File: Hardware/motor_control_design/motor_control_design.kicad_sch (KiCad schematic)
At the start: 40 parts, among them J1 TYPE-C-31-M-12, J2 SWD, J3 VBAT, J4 GND, J5 FC_M/P, U1 STM32F401CCU6, U2 AMS1117-3.3, U3 LM2576S-3.3, Y1 16MHz

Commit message: Added Vbat Sensing schema to motor board
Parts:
- added R11: 29.4k, Resistor_SMD:R_0402_1005Metric, symbol Device:R
- added R12: 10k, Resistor_SMD:R_0402_1005Metric, symbol Device:R
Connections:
- net +3.3V: now also U1.12 (PA2)
- net +BATT: now also R11.1
- net GND: now also R12.2
- net VBatt_sense: now reaches U1.11 (PA1)
- net VBatt_sense: now also R11.2, R12.1
- no-connect marks 35 -> 33
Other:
- note added: "*Calculated based off of 3S 18650 pack 18650: 2.5V -> 4.2V | 12.6v -> 3.198v pack : 7.5V -> 12.6v | 7.5v -> 1.904v ADC range is 0v -> 3.3v"
- note added: "*Need to test LM2576 voltage stability under ext. motor load, and heavy downstream load If needed, we may need to create a seperate power source for VREF+. Not sure how, but we could use a LM2576-5V then use a cheap 3.3V LDO and a high precsision one"
- note added: "Battery Voltage Measure"

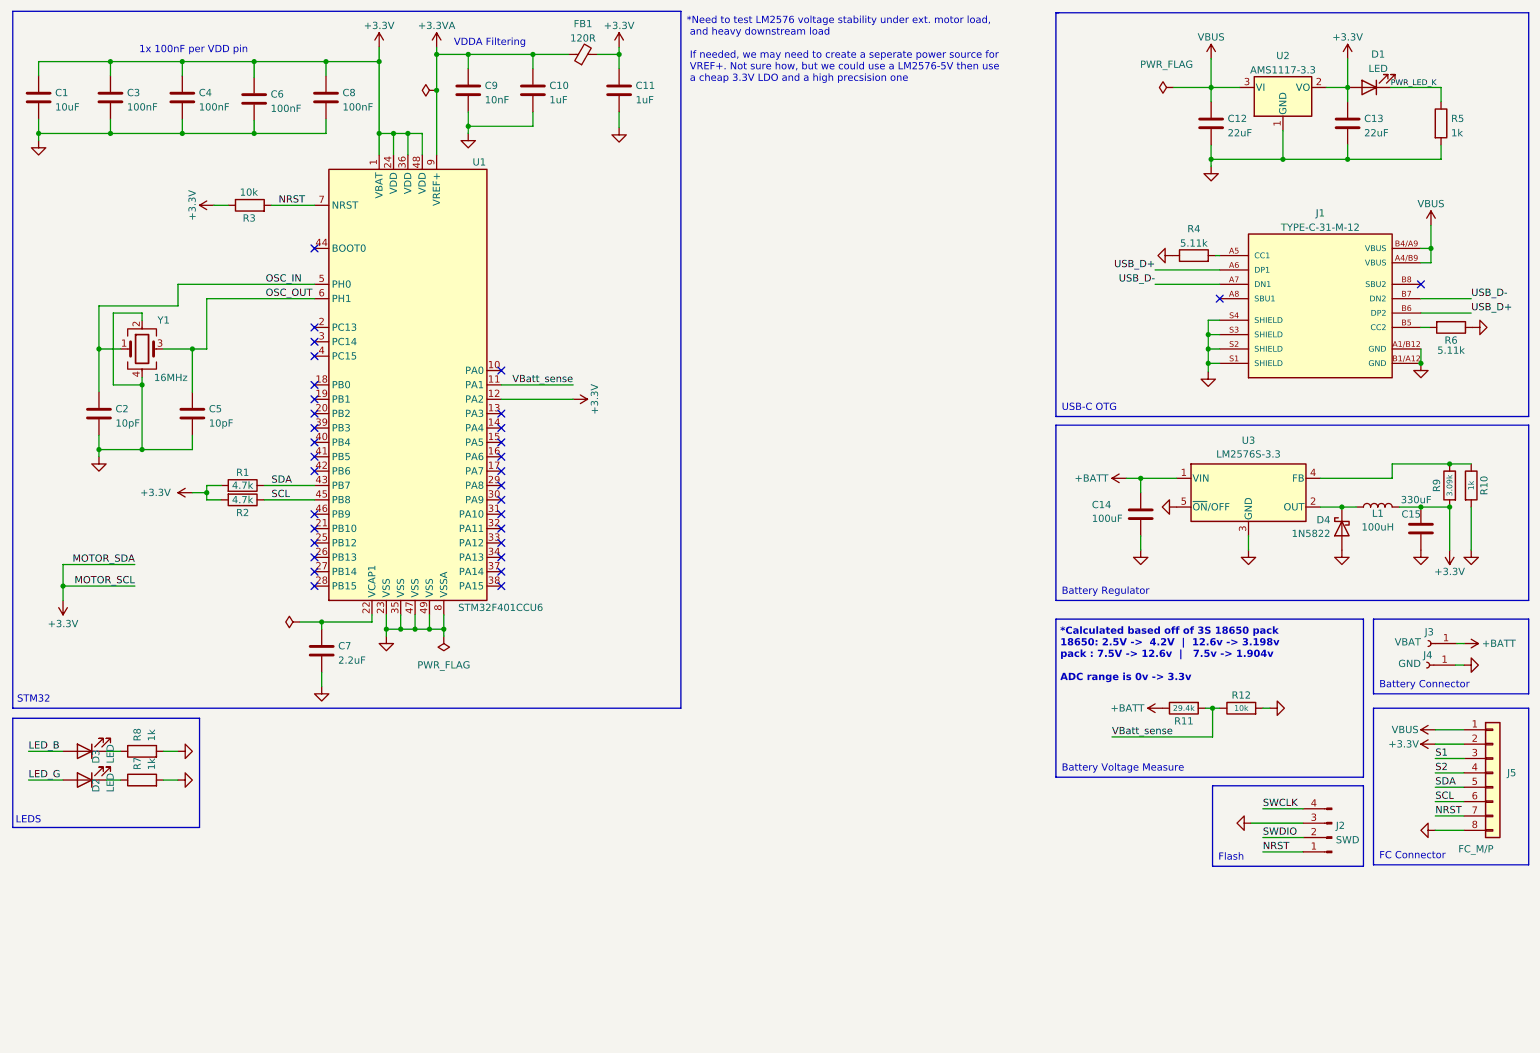
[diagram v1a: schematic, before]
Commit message: Added both H-Bridge schemas (pending testing)
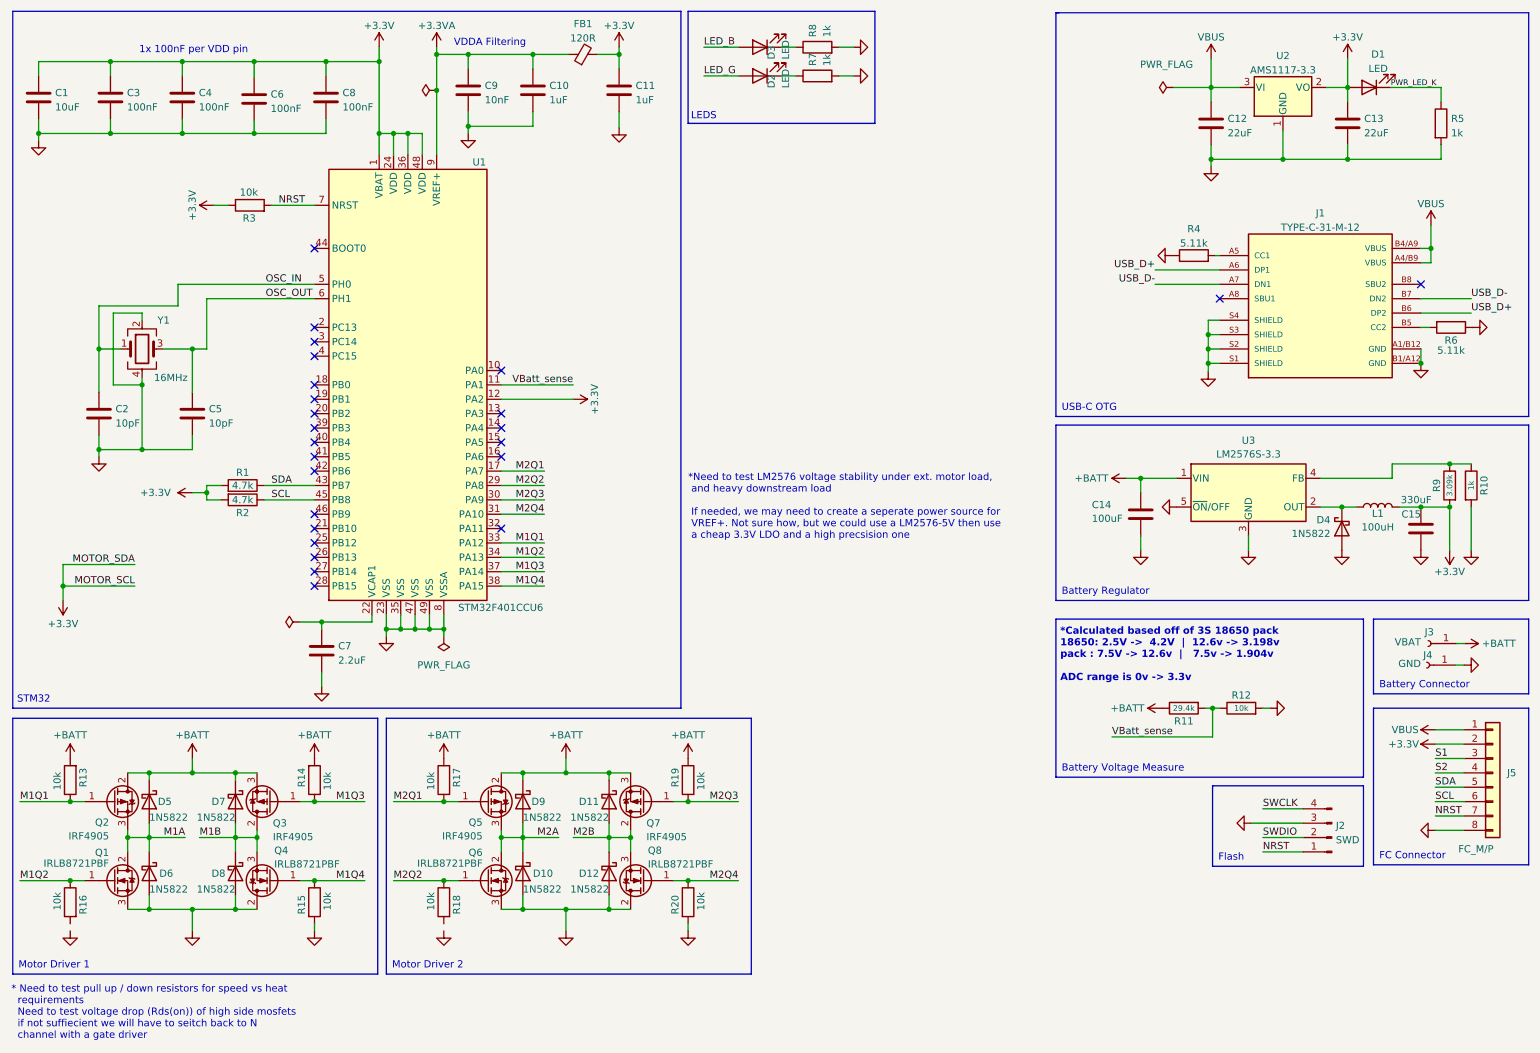
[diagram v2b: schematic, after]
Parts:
- added D10, D11, D12, D5, D6, D7, D8, D9: 1N5822, Diode_THT:D_DO-201AD_P15.24mm_Horizontal, symbol Diode:1N5822
- added Q1, Q4, Q6, Q8: IRLB8721PBF, Package_TO_SOT_THT:TO-220-3_Vertical, symbol Transistor_FET:IRLB8721PBF
- added Q2, Q3, Q5, Q7: IRF4905, Package_TO_SOT_THT:TO-220-3_Vertical, symbol Transistor_FET:IRF4905
- added R13, R14, R15, R16, R17, R18, R19, R20: 10k, Resistor_SMD:R_0402_1005Metric, symbol Device:R
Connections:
- net +BATT: now also D11.1 (K), D5.1 (K), D7.1 (K), D9.1 (K), Q2.2 (D), Q3.3 (S), Q5.2 (D), Q7.3 (S), R13.2, R14.2, R17.2, R19.2
- net GND: now also D10.2 (A), D12.2 (A), D6.2 (A), D8.2 (A), Q1.3 (S), Q4.2 (D), Q6.3 (S), Q8.2 (D), R15.2, R20.2
- net M2Q1: now reaches U1.17 (PA7)
- net M2Q1: now also Q5.1 (G), R17.1
- net M2Q2: now reaches U1.29 (PA8)
- net M2Q2: now also Q6.1 (G), R18.1
- net M2Q3: now reaches U1.30 (PA9)
- net M2Q3: now also Q7.1 (G), R19.1
- net M2Q4: now reaches U1.31 (PA10)
- net M2Q4: now also Q8.1 (G), R20.1
- net M1Q1: now reaches U1.33 (PA12)
- net M1Q1: now also Q2.1 (G), R13.1
- net M1Q2: now reaches U1.34 (PA13)
- net M1Q2: now also Q1.1 (G), R16.1
- net M1Q3: now reaches U1.37 (PA14)
- net M1Q3: now also Q3.1 (G), R14.1
- net M1Q4: now reaches U1.38 (PA15)
- net M1Q4: now also Q4.1 (G), R15.1
- new net M1A: D5.2 (A), D6.1 (K), Q1.2 (D), Q2.3 (S)
- new net M1B: D7.2 (A), D8.1 (K), Q3.2 (D), Q4.3 (S)
- new net M2A: D10.1 (K), D9.2 (A), Q5.3 (S), Q6.2 (D)
- new net M2B: D11.2 (A), D12.1 (K), Q7.2 (D), Q8.3 (S)
- no-connect marks 33 -> 25
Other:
- note added: "* Need to test pull up / down resistors for speed vs heat requirements Need to test voltage drop (Rds(on)) of high side mosfets if not suffiecient we will have to seitch back to N channel with a gate driver"
- note added: "Motor Driver 1"
- note added: "Motor Driver 2"
- moved on the sheet: D2, D3, R7, R8

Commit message: Finished motor controller schematic and routing
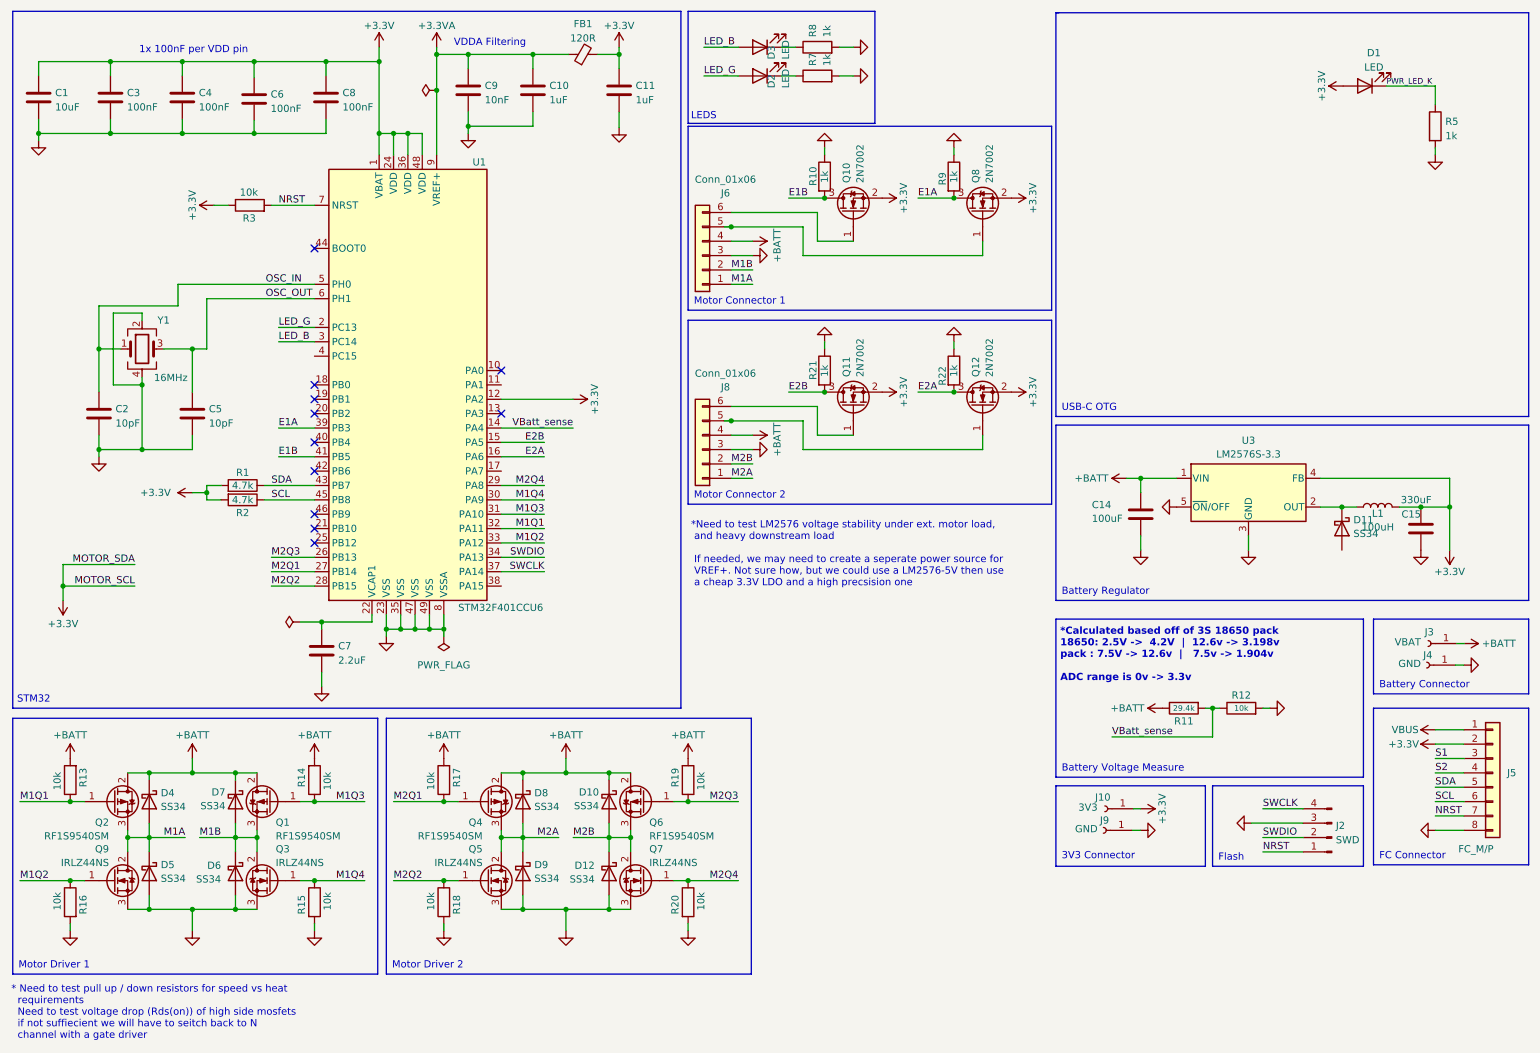
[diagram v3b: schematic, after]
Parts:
- removed C12, C13: 22uF, Capacitor_SMD:C_0805_2012Metric, symbol Device:C
- removed D10, D11, D12, D4, D5, D6, D7, D8, D9: 1N5822, Diode_THT:D_DO-201AD_P15.24mm_Horizontal, symbol Diode:1N5822
- removed J1: TYPE-C-31-M-12, USBC:HRO_TYPE-C-31-M-12, symbol TYPE-C-31-M-12:TYPE-C-31-M-12
- removed Q1, Q4, Q6, Q8: IRLB8721PBF, Package_TO_SOT_THT:TO-220-3_Vertical, symbol Transistor_FET:IRLB8721PBF
- removed Q3, Q5, Q7: IRF4905, Package_TO_SOT_THT:TO-220-3_Vertical, symbol Transistor_FET:IRF4905
- removed R4, R6: 5.11k, Resistor_SMD:R_0402_1005Metric, symbol Device:R
- removed U2: AMS1117-3.3, Package_TO_SOT_SMD:SOT-223-3_TabPin2, symbol Regulator_Linear:AMS1117-3.3
- added D10, D11, D12, D4, D5, D6, D7, D8, D9: SS34, Diode_SMD:D_SMA, symbol Diode:SS34
- added J10: 3V3, TestPoint:TestPoint_THTPad_4.0x4.0mm_Drill2.0mm, symbol Connector:Conn_01x01_Female
- added J6, J8: Conn_01x06, JST-XH-SMD:CONN_S6B-XH-SM4-TB_JST, symbol Connector_Generic:Conn_01x06
- added J9: GND, TestPoint:TestPoint_THTPad_4.0x4.0mm_Drill2.0mm, symbol Connector:Conn_01x01_Female
- added Q1, Q4, Q6: RF1S9540SM, Package_TO_SOT_SMD:TO-263-2, symbol Transistor_FET:IRF4905
- added Q10, Q11, Q12, Q8: 2N7002, Package_TO_SOT_SMD:SOT-23, symbol Transistor_FET:2N7002
- added Q3, Q5, Q7, Q9: IRLZ44NS, Package_TO_SOT_SMD:TO-263-2, symbol Transistor_FET:IRLZ44N
- added R21, R22: 1k, Resistor_SMD:R_0402_1005Metric, symbol Device:R
- C14: footprint Capacitor_SMD:C_0402_1005Metric -> Capacitor_SMD:C_0603_1608Metric
- J3, J4: footprint TestPoint:TestPoint_THTPad_2.5x2.5mm_Drill1.2mm -> TestPoint:TestPoint_THTPad_4.0x4.0mm_Drill2.0mm
- L1: footprint (none) -> Inductor_SMD:L_12x12mm_H4.5mm
- Q2: value IRF4905 -> RF1S9540SM; footprint Package_TO_SOT_THT:TO-220-3_Vertical -> Package_TO_SOT_SMD:TO-263-2
- R10: LCSC Part C25906 -> C11702
- R9: value 3.09k -> 1k; LCSC Part C25906 -> C11702
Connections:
- net +3.3V: now also U3.4 (FB), J10.1 (Pin_1), Q10.2 (S), Q11.2 (S), Q12.2 (S), Q8.2 (S); no longer R9.2
- net +BATT: now also D10.1 (K), D4.1 (K), D7.1 (K), D8.1 (K), J6.4 (Pin_4), J8.4 (Pin_4), Q1.2 (D), Q4.2 (D), Q6.2 (D)
- net GND: now also R10.1, R16.2, R18.2, R9.1, D12.2 (A), D5.2 (A), D6.2 (A), D9.2 (A), J6.3 (Pin_3), J8.3 (Pin_3), J9.1 (Pin_1), Q3.3 (S), Q5.3 (S), Q7.3 (S), Q9.3 (S), R21.1, R22.1; no longer R10.2
- net LED_B: now also U1.3 (PC14)
- net LED_G: now also U1.2 (PC13)
- net M1A: now also D4.2 (A), D5.1 (K), J6.1 (Pin_1), Q9.2 (D)
- net M1B: now also D6.1 (K), D7.2 (A), J6.2 (Pin_2), Q1.3 (S), Q3.2 (D)
- net M1Q1: now also U1.32 (PA11); no longer U1.33 (PA12)
- net M1Q2: now also U1.33 (PA12), Q9.1 (G); no longer U1.34 (PA13)
- net M1Q3: now also U1.31 (PA10), Q1.1 (G); no longer U1.37 (PA14)
- net M1Q4: now also U1.30 (PA9), Q3.1 (G); no longer U1.38 (PA15)
- net M2A: now also D8.2 (A), D9.1 (K), J8.1 (Pin_1), Q4.3 (S), Q5.2 (D)
- net M2B: now also D10.2 (A), D12.1 (K), J8.2 (Pin_2), Q6.3 (S), Q7.2 (D)
- net M2Q1: now also U1.27 (PB14), Q4.1 (G); no longer U1.17 (PA7)
- net M2Q2: now also U1.28 (PB15), Q5.1 (G); no longer U1.29 (PA8)
- net M2Q3: now also U1.26 (PB13), Q6.1 (G); no longer U1.30 (PA9)
- net M2Q4: now also U1.29 (PA8), Q7.1 (G); no longer U1.31 (PA10)
- net SWCLK: now also U1.37 (PA14)
- net SWDIO: now also U1.34 (PA13)
- net VBatt_sense: now also U1.14 (PA4); no longer U1.11 (PA1)
- net at L1.1, U3.2 (OUT): now also D11.1 (K)
- net E2B: now reaches U1.15 (PA5)
- net E2B: now also Q11.3 (D), R21.2
- net E2A: now reaches U1.16 (PA6)
- net E2A: now also Q12.3 (D), R22.2
- net E1A: now reaches U1.39 (PB3)
- net E1A: now also R9.2, Q8.3 (D)
- net E1B: now reaches U1.41 (PB5)
- net E1B: now also R10.2, Q10.3 (D)
- new net: J8.6 (Pin_6), Q11.1 (G)
- new net: J6.6 (Pin_6), Q10.1 (G)
- new net: J6.5 (Pin_5), Q8.1 (G)
- new net: J8.5 (Pin_5), Q12.1 (G)
- no-connect marks 25 -> 11
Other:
- note added: "3V3 Connector"
- note added: "Motor Connector 1"
- note added: "Motor Connector 2"
- moved on the sheet: D1, R5
